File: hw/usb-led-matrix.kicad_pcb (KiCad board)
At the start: 2 copper layers, 76 parts, among them J2 Conn_ARM_JTAG_SWD_10, U1 AP1117-33, U2 stm32g473, U3 74LVT244A

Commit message: Updates
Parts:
- added C1: C, Capacitor_SMD:C_0402_1005Metric_Pad0.74x0.62mm_HandSolder, F.Cu at (181.5, 107.5)
- added C2: C, Capacitor_SMD:C_0402_1005Metric_Pad0.74x0.62mm_HandSolder, F.Cu at (177.0, 94.5)
- added C3: C, Capacitor_SMD:C_0402_1005Metric_Pad0.74x0.62mm_HandSolder, F.Cu at (186.5, 98.0)
- added C4: C, Capacitor_SMD:C_0402_1005Metric_Pad0.74x0.62mm_HandSolder, F.Cu at (183.0, 107.5)
- added C5: C, Capacitor_SMD:C_0603_1608Metric_Pad1.08x0.95mm_HandSolder, F.Cu at (184.5, 91.0)
- added C6: C, Capacitor_SMD:C_0603_1608Metric_Pad1.08x0.95mm_HandSolder, F.Cu at (181.0, 91.0)
- added C7: C, Capacitor_SMD:C_0402_1005Metric_Pad0.74x0.62mm_HandSolder, F.Cu at (171.5, 88.5)
- added J1: Conn_01x04_Male, Connector_PinHeader_1.27mm:PinHeader_1x04_P1.27mm_Vertical, F.Cu at (186.0, 105.0)
- added R9: R, Resistor_SMD:R_0402_1005Metric_Pad0.72x0.64mm_HandSolder, F.Cu at (178.5, 94.5)
- added Y1: Crystal_GND23, Crystal:Crystal_SMD_3225-4Pin_3.2x2.5mm_HandSoldering, F.Cu at (173.0, 94.5)
- U3: value 74LVT244A -> 74LVT245; footprint Package_SO:SOIC-20W_7.5x12.8mm_P1.27mm -> Package_SO:TSSOP-20_4.4x6.5mm_P0.65mm
- moved D2 33.2 mm to (142.0, 85.5), turned to 45 degrees
- moved D25 33.1 mm to (152.5, 82.0), turned to 45 degrees
- moved R4 32.8 mm to (172.0, 102.0)
- moved U3 30.8 mm to (173.5, 84.5), turned to 180 degrees
- moved D58 30.7 mm to (166.5, 85.5), turned to 45 degrees
- moved R3 30.4 mm to (172.0, 101.0)
- moved J2 29.1 mm to (174.5, 109.0), turned to 90 degrees
- moved R1 28.9 mm to (172.0, 99.0)
- moved D35 28.1 mm to (156.0, 89.0), turned to 45 degrees
- moved D40 27.8 mm to (156.0, 106.5), turned to 45 degrees
- moved U2 26.3 mm to (180.0, 101.0)
- moved R2 25.0 mm to (172.0, 100.0)
- moved R8 24.9 mm to (172.0, 106.0)
- moved D45 24.9 mm to (159.5, 96.0), turned to 45 degrees
- moved D24 24.8 mm to (149.0, 106.5), turned to 45 degrees
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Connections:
- J2 pad 1: Net-(J2-Pad1) -> /VDD
- J2 pad 10: Net-(J2-Pad10) -> /NRST
- J2 pad 2: Net-(J2-Pad2) -> /SWDIO
- J2 pad 3: Net-(J2-Pad3) -> GND
- J2 pad 4: Net-(J2-Pad4) -> /SWCLK
- J2 pad 5: Net-(J2-Pad3) -> GND
- J2 pad 9: Net-(J2-Pad9) -> GND
- U1 pad 1: Net-(U1-Pad1) -> GND
- U1 pad 2: Net-(U1-Pad2) -> /VDD
- U2 pad 19: Net-(U2-Pad19) -> GND
- U2 pad 21: Net-(U2-Pad21) -> /VDD
- U2 pad 23: Net-(U2-Pad23) -> GND
- U2 pad 24: Net-(U2-Pad24) -> /VDD
- U2 pad 35: Net-(U2-Pad35) -> GND
- U2 pad 36: Net-(U2-Pad36) -> /VDD
- U2 pad 45: Net-(U2-Pad45) -> /BOOT0
- U2 pad 47: Net-(U2-Pad47) -> GND
- U2 pad 48: Net-(U2-Pad48) -> /VDD
- U2 pad 7: Net-(U2-Pad7) -> /NRST
- U3 pad 10: Net-(U3-Pad10) -> GND
- U3 pad 11: /COL1 -> Net-(D1-Pad1)
- U3 pad 12: Net-(D33-Pad1) -> Net-(D10-Pad1)
- U3 pad 13: /COL2 -> Net-(D17-Pad1)
- U3 pad 14: Net-(D41-Pad1) -> Net-(D25-Pad1)
- U3 pad 15: /COL3 -> Net-(D33-Pad1)
- U3 pad 16: Net-(D49-Pad1) -> Net-(D41-Pad1)
- U3 pad 17: /COL4 -> Net-(D49-Pad1)
- U3 pad 20: Net-(U3-Pad20) -> /VDD
- U3 pad 3: Net-(D25-Pad1) -> /COL7
- U3 pad 4: /COL7 -> /COL6
- U3 pad 5: Net-(D17-Pad1) -> /COL5
- U3 pad 6: /COL6 -> /COL4
- U3 pad 7: Net-(D10-Pad1) -> /COL3
- U3 pad 8: /COL5 -> /COL2
- U3 pad 9: Net-(D1-Pad1) -> /COL1
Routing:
- net Net-(D17-Pad1): track 0.00 -> 36.1 mm, vias 0 -> 8
- net Net-(D10-Pad1): track 0.00 -> 36.1 mm, vias 0 -> 8
- net Net-(D16-Pad2): track 0.00 -> 24.5 mm
- net Net-(D15-Pad2): track 0.00 -> 24.5 mm
- net Net-(D14-Pad2): track 0.00 -> 24.5 mm
- net Net-(D13-Pad2): track 0.00 -> 24.5 mm
- net Net-(D12-Pad2): track 0.00 -> 24.5 mm
- net Net-(D11-Pad2): track 0.00 -> 24.5 mm
- net Net-(D10-Pad2): track 0.00 -> 24.5 mm
- net Net-(D1-Pad2): track 0.00 -> 24.5 mm
- net Net-(D1-Pad1): track 0.00 -> 24.5 mm
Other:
- board outline added: 60 x 30 mm
- net class Default: trace_width 0.25 -> 0.16
- net class Power added: clearance 0.2, trace_width 0.3, via_dia 0.8, via_drill 0.4
- rule trace_min: 0.2 -> 0.15

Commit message: Work
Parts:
- removed J1: Conn_01x04_Male, Connector_PinHeader_1.27mm:PinHeader_1x04_P1.27mm_Vertical
- added C8: C, Capacitor_SMD:C_0603_1608Metric_Pad1.08x0.95mm_HandSolder, F.Cu at (181.8, 108.8)
- added C9: C, Capacitor_SMD:C_0402_1005Metric_Pad0.74x0.62mm_HandSolder, F.Cu at (178.8, 108.8)
- added J3: USB_A, usb-board-edge:usb-a-board-edge, F.Cu at (195.0, 95.0)
- added TP1: TestPoint, TestPoint:TestPoint_THTPad_D1.0mm_Drill0.5mm, F.Cu at (178.6, 92.2)
- added TP2: TestPoint, TestPoint:TestPoint_THTPad_D1.0mm_Drill0.5mm, F.Cu at (178.6, 94.2)
- added TP3: TestPoint, TestPoint:TestPoint_THTPad_D1.0mm_Drill0.5mm, F.Cu at (178.6, 96.2)
- J2: value Conn_ARM_JTAG_SWD_10 -> Conn_ST_STDC14; footprint Connector_PinHeader_1.27mm:PinHeader_2x05_P1.27mm_Vertical -> Connector_PinHeader_1.27mm:PinHeader_2x07_P1.27mm_Vertical_SMD; moved to B.Cu
- U2: value stm32g473 -> STM32G473CET6
- Y1: value Crystal_GND23 -> Crystal_GND24; footprint Crystal:Crystal_SMD_3225-4Pin_3.2x2.5mm_HandSoldering -> Crystal:Crystal_SMD_3225-4Pin_3.2x2.5mm
- moved C6 10.1 mm to (186.6, 82.6), turned to 270 degrees
- moved J2 6.80 mm to (180.0, 105.0), turned to 270 degrees
- moved C5 4.17 mm to (186.6, 87.4), turned to 90 degrees
- moved C1 3.14 mm to (184.6, 108.0), turned to 0 degrees
- moved C2 2.42 mm to (175.8, 96.6)
- moved Y1 2.14 mm to (173.4, 96.6)
- moved R9 1.73 mm to (180.2, 94.2)
- moved C4 1.68 mm to (184.6, 107.0), turned to 0 degrees
- moved R1 1.60 mm to (172.0, 100.6)
- moved R2 1.60 mm to (172.0, 101.6)
- moved R3 1.60 mm to (172.0, 102.6)
- moved R4 1.60 mm to (172.0, 103.6)
- moved R5 1.60 mm to (172.0, 104.6)
- moved R6 1.60 mm to (172.0, 105.6)
- moved R7 1.60 mm to (172.0, 106.6)
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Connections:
- net Net-(C5-Pad1) renamed /VBUS
- J2 pad 1: /VDD -> Net-(J2-Pad1)
- J2 pad 10: /NRST -> Net-(J2-Pad10)
- J2 pad 2: /SWDIO -> Net-(J2-Pad2)
- J2 pad 3: GND -> /VDD
- J2 pad 4: /SWCLK -> /SWDIO
- J2 pad 6: Net-(J2-Pad6) -> /SWCLK
- J2 pad 7: Net-(J2-Pad7) -> GND
- J2 pad 9: GND -> Net-(J2-Pad9)
- R9 pad 1: Net-(R9-Pad1) -> GND
- U2 pad 31: Net-(U2-Pad31) -> /TX
- U2 pad 32: Net-(U2-Pad32) -> /RX
- U3 pad 1: Net-(U3-Pad1) -> /VDD
- U3 pad 19: Net-(U3-Pad19) -> GND
- Y1 pad 2: Net-(Y1-Pad2) -> GND
- Y1 pad 3: Net-(Y1-Pad3) -> Net-(U2-Pad6)
- Y1 pad 4: Net-(U2-Pad6) -> GND
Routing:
- net /VDD: track 0.00 -> 87.2 mm, vias 0 -> 3
- net GND: track 0.00 -> 38.9 mm, vias 0 -> 21
- net Net-(D1-Pad1): track 24.5 -> 55.9 mm
- net /COL1: track 0.00 -> 29.2 mm, vias 0 -> 2
- net /COL2: track 0.00 -> 28.3 mm, vias 0 -> 2
- net Net-(D10-Pad1): track 36.1 -> 63.8 mm, vias 8 -> 9
- net /COL3: track 0.00 -> 27.2 mm, vias 0 -> 2
- net Net-(D17-Pad1): track 36.1 -> 59.9 mm, vias 8 -> 9
- net Net-(D1-Pad2): track 24.5 -> 44.7 mm
- net /COL4: track 0.00 -> 18.8 mm
- net Net-(D10-Pad2): track 24.5 -> 43.2 mm
- net /COL8: track 0.00 -> 18.6 mm
- net /COL5: track 0.00 -> 18.1 mm
- net /COL6: track 0.00 -> 17.0 mm
- net /COL7: track 0.00 -> 16.3 mm
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- added copper zone on F.Cu, net /VDD
- added copper zone on B.Cu, net GND
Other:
- outline, holes or cut-outs redrawn
- net class Default: clearance 0.2 -> 0.16; via_dia 0.8 -> 0.6; via_drill 0.4 -> 0.3
- net class Power: clearance 0.2 -> 0.16; via_dia 0.8 -> 0.6; via_drill 0.4 -> 0.3
- net class USB added: clearance 0.2, trace_width 0.2, via_dia 0.6, via_drill 0.3
- rule trace_clearance: 0.2 -> 0.16
- rule trace_min: 0.15 -> 0.1
- rule via_min_size: 0.4 -> 0.6

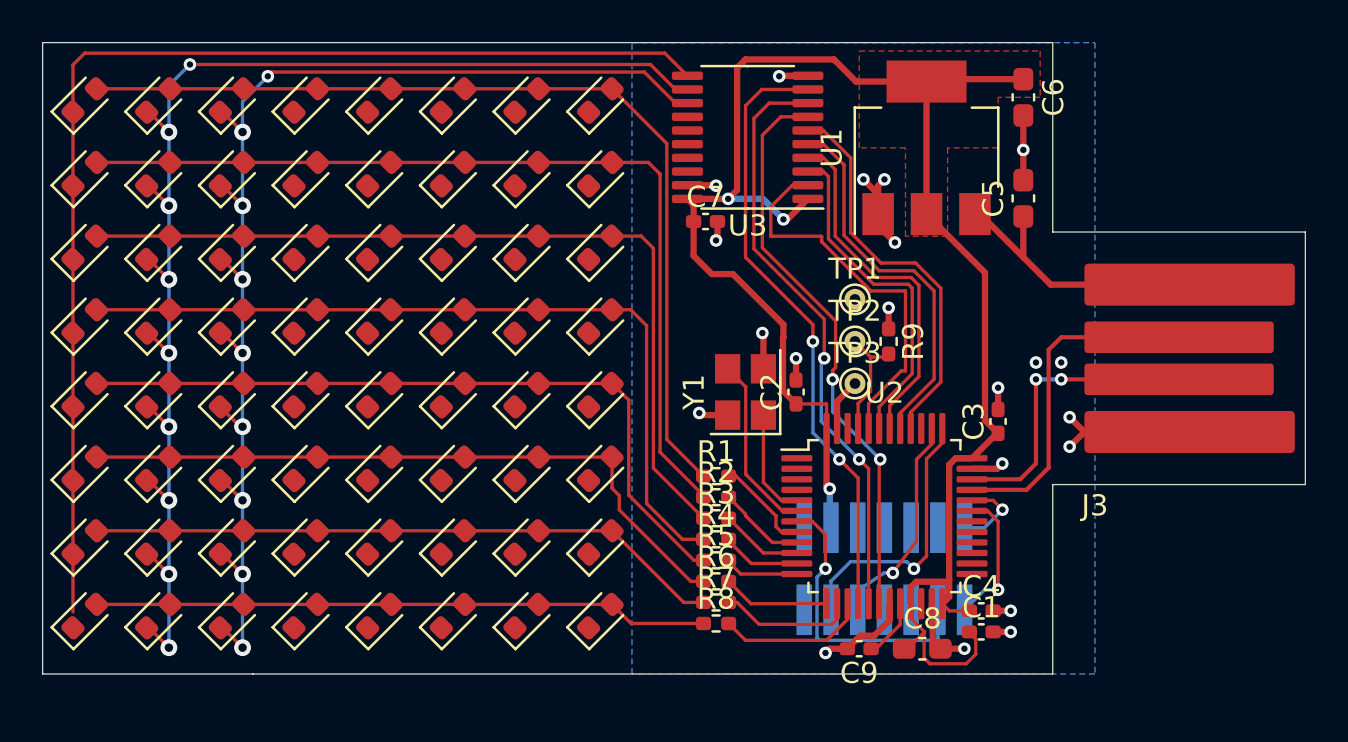
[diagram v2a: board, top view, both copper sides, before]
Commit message: Four-layer board, update routing and some components
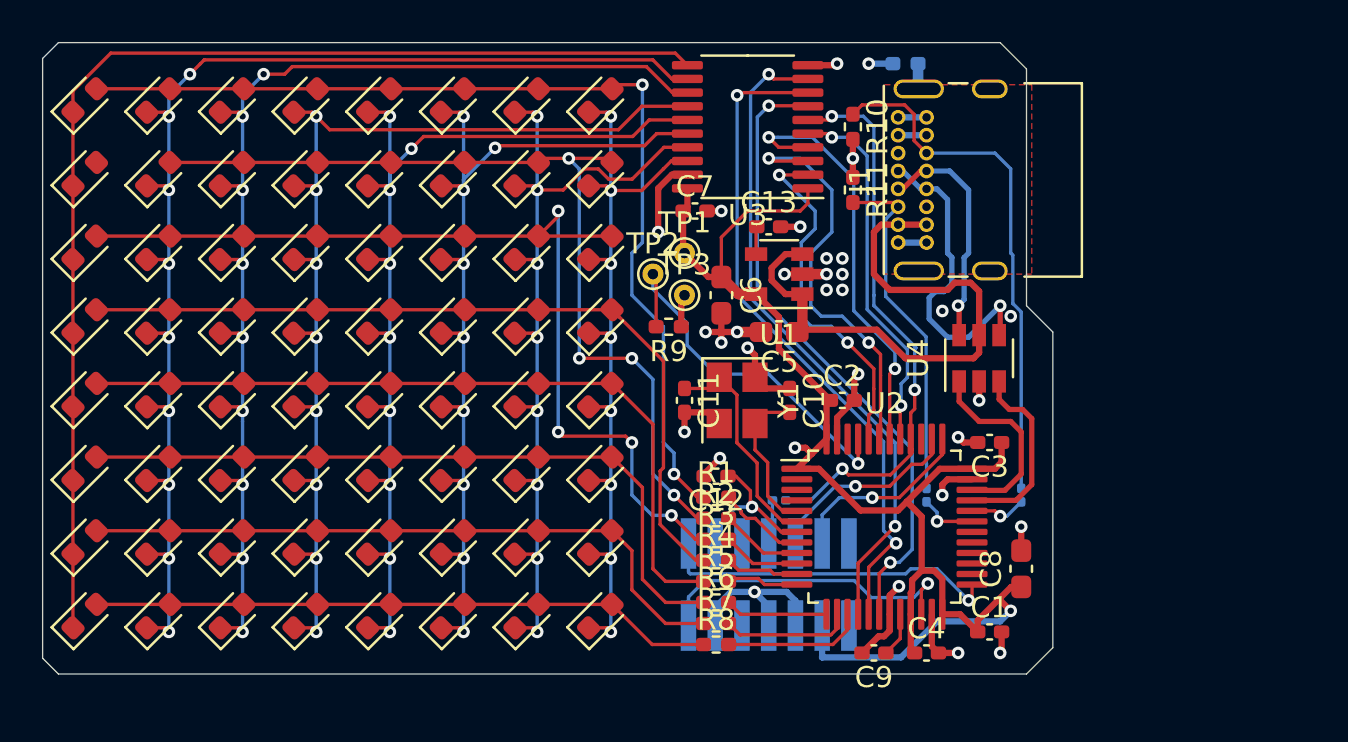
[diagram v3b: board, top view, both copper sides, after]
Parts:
- removed J3: USB_A, usb-board-edge:usb-a-board-edge
- added C10: p, Capacitor_SMD:C_0402_1005Metric_Pad0.74x0.62mm_HandSolder, F.Cu at (175.5, 97.0)
- added C11: p, Capacitor_SMD:C_0402_1005Metric_Pad0.74x0.62mm_HandSolder, F.Cu at (170.5, 97.0)
- added C12: 100n, Capacitor_SMD:C_0402_1005Metric_Pad0.74x0.62mm_HandSolder, F.Cu at (172.0, 100.6)
- added C13: DNP, Capacitor_SMD:C_0402_1005Metric_Pad0.74x0.62mm_HandSolder, F.Cu at (174.5, 88.8)
- added J1: USB_C_Receptacle_USB2.0, Connector_USB:USB_C_Receptacle_GCT_USB4085, F.Cu at (180.7, 89.5)
- added NT1: Net-Tie_2, Resistor_SMD:R_0201_0603Metric, B.Cu at (175.0, 101.8)
- added NT2: Net-Tie_2, Resistor_SMD:R_0201_0603Metric, B.Cu at (182.0, 101.5)
- added NT3: Net-Tie_2, Resistor_SMD:R_0201_0603Metric, B.Cu at (186.5, 101.5)
- added R10: 5k1, Resistor_SMD:R_0402_1005Metric_Pad0.72x0.64mm_HandSolder, F.Cu at (178.5, 84.0)
- added R11: 5k1, Resistor_SMD:R_0402_1005Metric_Pad0.72x0.64mm_HandSolder, F.Cu at (178.5, 87.0)
- added R12: DNP, Resistor_SMD:R_0402_1005Metric_Pad0.72x0.64mm_HandSolder, B.Cu at (181.0, 81.0)
- added U4: USBLC6-2SC6, Package_TO_SOT_SMD:SOT-23-6, F.Cu at (184.5, 95.0)
- C1, C2, C3, C4, C7: value C -> 100n
- C5: value C -> 1u
- C6: value C -> 10u
- C8: value C -> 4.7u
- C9: value C -> DNP
- U1: value AP1117-33 -> AP2210K-3.3; footprint Package_TO_SOT_SMD:SOT-223-3_TabPin2 -> Package_TO_SOT_SMD:SOT-23-5
- moved C6 17.2 mm to (172.2, 92.0)
- moved C5 13.2 mm to (175.0, 93.8), turned to 180 degrees
- moved R9 10.5 mm to (169.8, 93.5), turned to 180 degrees
- moved TP2 10.1 mm to (169.0, 91.0)
- moved U1 9.22 mm to (175.0, 91.0), turned to 180 degrees
- moved TP3 9.12 mm to (170.5, 92.0)
- moved TP1 8.39 mm to (170.5, 90.0)
- moved C8 6.04 mm to (186.5, 105.0), turned to 90 degrees
- moved J2 5.55 mm to (174.5, 105.8), turned to 90 degrees
- moved C4 3.28 mm to (182.0, 109.0)
- moved C2 2.24 mm to (178.0, 97.0), turned to 0 degrees
- moved C3 1.08 mm to (185.0, 99.0), turned to 180 degrees
- moved R1 1.00 mm to (172.0, 101.6)
- moved R2 1.00 mm to (172.0, 102.6)
- moved R3 1.00 mm to (172.0, 103.6)
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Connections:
- net Net-(C9-Pad1) renamed /VREF+
- J2 pad 1: Net-(J2-Pad1) -> (no net)
- J2 pad 10: Net-(J2-Pad10) -> (no net)
- J2 pad 2: Net-(J2-Pad2) -> (no net)
- J2 pad 9: Net-(J2-Pad9) -> (no net)
- U1 pad 1: GND -> /VBUS
- U1 pad 2: /VDD -> GND
- U2 pad 1: Net-(U2-Pad1) -> /VDD
- U2 pad 2: Net-(U2-Pad2) -> (no net)
- U2 pad 22: Net-(U2-Pad22) -> /RX
- U2 pad 25: Net-(U2-Pad25) -> /TX
- U2 pad 26: Net-(U2-Pad26) -> (no net)
- U2 pad 27: Net-(U2-Pad27) -> (no net)
- U2 pad 28: Net-(U2-Pad28) -> (no net)
- U2 pad 29: Net-(U2-Pad29) -> (no net)
- U2 pad 3: Net-(U2-Pad3) -> (no net)
- U2 pad 30: Net-(U2-Pad30) -> (no net)
- U2 pad 31: /TX -> /USB_CC1
- U2 pad 32: /RX -> /USB_CC2
- U2 pad 39: Net-(U2-Pad39) -> (no net)
- U2 pad 4: Net-(U2-Pad4) -> (no net)
- U2 pad 46: Net-(U2-Pad46) -> (no net)
- U2 pad 5: Net-(U2-Pad5) -> Net-(C10-Pad2)
- U2 pad 6: Net-(U2-Pad6) -> Net-(C11-Pad1)
- Y1 pad 1: Net-(U2-Pad5) -> Net-(C11-Pad1)
- Y1 pad 3: Net-(U2-Pad6) -> Net-(C10-Pad2)
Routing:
- net Net-(D25-Pad1): track 0.00 -> 52.0 mm, vias 0 -> 8
- net Net-(D33-Pad1): track 0.00 -> 49.7 mm, vias 0 -> 9
- net Net-(D41-Pad1): track 0.00 -> 45.6 mm, vias 0 -> 9
- net Net-(D49-Pad1): track 0.00 -> 42.0 mm, vias 0 -> 8
- net Net-(D57-Pad1): track 0.00 -> 37.8 mm, vias 0 -> 8
- net Net-(J1-PadB5): track 0.00 -> 25.1 mm
- net /VDD: track 87.2 -> 66.8 mm, vias 3 -> 2
- net Net-(J1-PadA5): track 0.00 -> 16.7 mm
- net /VBUS: track 13.5 -> 29.8 mm
- net /USB_DM_CON: track 0.00 -> 15.1 mm, vias 0 -> 1
- net GND: track 38.9 -> 51.9 mm, vias 21 -> 30
- net /BOOT0: track 5.61 -> 18.4 mm, vias 0 -> 1
- net /RX: track 3.78 -> 15.3 mm
- net /USB_DP_CON: track 0.00 -> 11.2 mm, vias 0 -> 1
- net Net-(C11-Pad1): track 0.00 -> 10.6 mm
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- added copper zone on F.Cu, net /SHIELD
- added copper zone on In1.Cu, net GND
- added copper zone on In2.Cu, net GND
- removed copper zone on F.Cu, net /VDD
- removed copper zone on B.Cu, net GND
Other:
- board size 60 x 30 mm -> 48 x 30 mm
- copper layers 2 -> 4
- net class USB: trace_width 0.2 -> 0.25
- rule via_min_drill: 0.3 -> 0.2
- rule via_min_size: 0.6 -> 0.4

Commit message: Rearrange pins
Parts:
- removed NT1: Net-Tie_2, Resistor_SMD:R_0201_0603Metric
- J1: value USB_C_Receptacle_USB2.0 -> USB4085-GF-A
- NT2, NT3: moved to F.Cu
- R1, R2, R3, R4, R5, R6, R7, R8: value R -> 68
- Y1: value Crystal_GND24 -> ABM8-24.000MHZ-B2-T
- moved J2 6.21 mm to (178.5, 101.0), turned to 180 degrees
- moved NT2 4.27 mm to (186.0, 103.0), turned to 180 degrees
- moved C8 3.88 mm to (185.5, 108.8), turned to 0 degrees
- moved C12 1.00 mm to (171.0, 100.6)
- moved R1 1.00 mm to (171.0, 101.6)
- moved R2 1.00 mm to (171.0, 102.6)
- moved R3 1.00 mm to (171.0, 103.6)
- moved R4 1.00 mm to (171.0, 104.6)
- moved R5 1.00 mm to (171.0, 105.6)
- moved R6 1.00 mm to (171.0, 106.6)
- moved R7 1.00 mm to (171.0, 107.6)
- moved R8 1.00 mm to (171.0, 108.6)
- moved NT3 0.90 mm to (186.0, 102.2), turned to 180 degrees
- moved C1 0.50 mm to (185.0, 107.5)
- moved C13 0.25 mm to (174.5, 88.5)
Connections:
- J2 pad 8: Net-(J2-Pad8) -> (no net)
- R9 pad 2: /BOOT0 -> /ROW1
- TP2 pad 1: /BOOT0 -> /ROW1
- U2 pad 10: /ROW3 -> /TX
- U2 pad 11: /ROW4 -> /RX
- U2 pad 12: /ROW5 -> (no net)
- U2 pad 13: /ROW6 -> (no net)
- U2 pad 14: /ROW7 -> (no net)
- U2 pad 15: /ROW8 -> (no net)
- U2 pad 22: /RX -> /ROW3
- U2 pad 25: /TX -> /ROW4
- U2 pad 26: (no net) -> /ROW5
- U2 pad 27: (no net) -> /ROW6
- U2 pad 28: (no net) -> /ROW7
- U2 pad 29: (no net) -> /ROW8
- U2 pad 45: /BOOT0 -> /ROW1
- U2 pad 46: (no net) -> /ROW2
- U2 pad 8: /ROW1 -> (no net)
- U2 pad 9: /ROW2 -> (no net)
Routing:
- net /ROW1: track 4.22 -> 25.1 mm, vias 0 -> 2
- net /BOOT0: track 18.4 -> 0.00 mm, vias 1 -> 0
- net /ROW8: track 6.68 -> 22.5 mm, vias 0 -> 2
- net /ROW7: track 6.18 -> 20.8 mm, vias 0 -> 2
- net /ROW6: track 4.89 -> 19.5 mm, vias 0 -> 2
- net /ROW5: track 3.42 -> 18.0 mm, vias 0 -> 2
- net /ROW4: track 3.51 -> 17.2 mm, vias 0 -> 2
- net /TX: track 16.2 -> 3.16 mm
- net /ROW3: track 3.72 -> 13.9 mm, vias 0 -> 2
- net /RX: track 15.3 -> 6.56 mm
- net /SWCLK: track 9.45 -> 17.9 mm
- net /COL4: track 27.0 -> 18.8 mm, vias 3 -> 2
- net Net-(J1-PadA5): track 16.7 -> 24.3 mm, vias 0 -> 1
- net /ROW2: track 3.92 -> 10.8 mm, vias 0 -> 2
- net /SWDIO: track 8.99 -> 15.3 mm
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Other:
- net class Default: clearance 0.16 -> 0.15
- net class Power: clearance 0.16 -> 0.15
- net class Tight added: clearance 0.12, trace_width 0.12, via_dia 0.5, via_drill 0.2
- net class USB: clearance 0.2 -> 0.15
- rule trace_clearance: 0.16 -> 0.15

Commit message: Update routing
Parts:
- added R13: R, Resistor_SMD:R_0402_1005Metric_Pad0.72x0.64mm_HandSolder, F.Cu at (169.0, 88.5)
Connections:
- net /USB_DM renamed /USB_D-
- net /USB_DM_CON renamed /USBCON_D-
- net /USB_DP renamed /USB_D+
- net /USB_DP_CON renamed /USBCON_D+
- U2 pad 8: (no net) -> /BUFFER_EN
- U3 pad 19: GND -> /BUFFER_EN
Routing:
- net /BUFFER_EN: track 0.00 -> 30.6 mm, vias 0 -> 2
- net /VBUS: track 29.7 -> 25.1 mm
- net GND: track 49.6 -> 46.7 mm
- net /VDD: track 69.3 -> 71.2 mm
- net /ROW8: track 22.5 -> 24.2 mm
- net /USBCON_D-: track 14.5 -> 12.9 mm
- net /ROW2: track 10.8 -> 11.7 mm
- net /ROW3: track 13.9 -> 13.1 mm
- net /ROW7: track 20.8 -> 21.5 mm
- added copper zone on F.Cu, net GND
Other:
- net class USB: clearance 0.15 -> 0.2

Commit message: PCB updates
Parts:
- added G***: LOGO, elemental:elemental-4mm, F.Cu at (180.2, 94.2)
- added G***: LOGO, elemental:elemental-25.4mm, B.Cu at (146.2, 94.8)
- added REF**: gnome1, Jonas_Gnomes:gnome1, B.Cu at (172.2, 85.0)
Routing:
- net /VBUS: track 25.1 -> 31.5 mm
- net Net-(D10-Pad2): track 42.6 -> 46.1 mm
- added copper zone on B.Cu, net GND
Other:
- board text added: "+3.3V"
- board text added: "1"
- board text added: "BOOT0"
- board text added: "GND"

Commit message: Fine tune PCB, silkscreen rev.A
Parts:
- removed REF**: gnome1, Jonas_Gnomes:gnome1
- added TP4: TestPoint, TestPoint:TestPoint_Pad_1.0x1.0mm, F.Cu at (173.5, 107.0)
- added TP5: TestPoint, TestPoint:TestPoint_Pad_1.0x1.0mm, F.Cu at (173.5, 108.5)
- added TP6: TestPoint, TestPoint:TestPoint_Pad_1.0x1.0mm, F.Cu at (175.0, 107.0)
- added TP7: TestPoint, TestPoint:TestPoint_Pad_1.0x1.0mm, F.Cu at (175.0, 108.5)
- Y1: footprint Crystal:Crystal_SMD_3225-4Pin_3.2x2.5mm -> jonas_Crystal:Crystal_SMD_3225-4Pin_3.2x2.5mm
- moved G*** 1.25 mm to (145.0, 94.8)
- moved G*** 0.56 mm to (180.8, 94.5), turned to 90 degrees
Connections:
- U2 pad 12: (no net) -> Net-(TP4-Pad1)
- U2 pad 13: (no net) -> Net-(TP6-Pad1)
- U2 pad 14: (no net) -> Net-(TP5-Pad1)
- U2 pad 15: (no net) -> Net-(TP7-Pad1)
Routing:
- net GND: track 46.7 -> 57.0 mm, vias 31 -> 40
- net Net-(TP5-Pad1): track 0.00 -> 5.55 mm
- net Net-(TP7-Pad1): track 0.00 -> 4.44 mm
- net Net-(TP4-Pad1): track 0.00 -> 3.29 mm
- net /SWCLK: track 17.7 -> 20.2 mm
- net Net-(TP6-Pad1): track 0.00 -> 2.32 mm
- net Net-(D11-Pad2): track 46.2 -> 47.5 mm
- net /SWDIO: track 15.3 -> 16.5 mm
- net Net-(D1-Pad2): track 47.4 -> 48.4 mm
- net /VBUS: track 31.5 -> 32.4 mm
- net /COL3: track 28.7 -> 29.5 mm
- net /ROW1: track 25.5 -> 24.8 mm
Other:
- outline, holes or cut-outs redrawn
- board text added: "2021"
- board text added: "Jonas Norling"
- board text added: "rev.A"
